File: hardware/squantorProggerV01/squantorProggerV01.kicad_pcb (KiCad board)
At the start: 2 copper layers, 29 x 29 mm, 4 parts

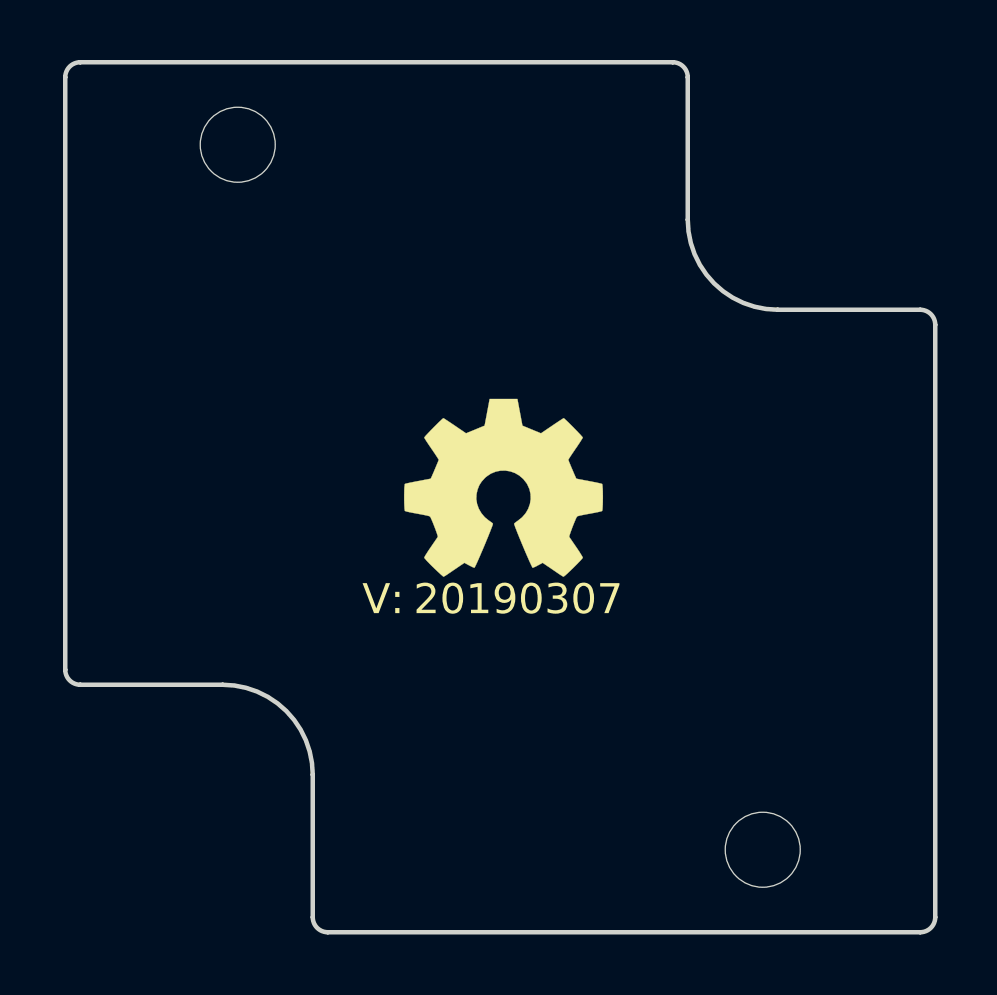
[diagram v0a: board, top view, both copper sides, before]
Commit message: placed connectors
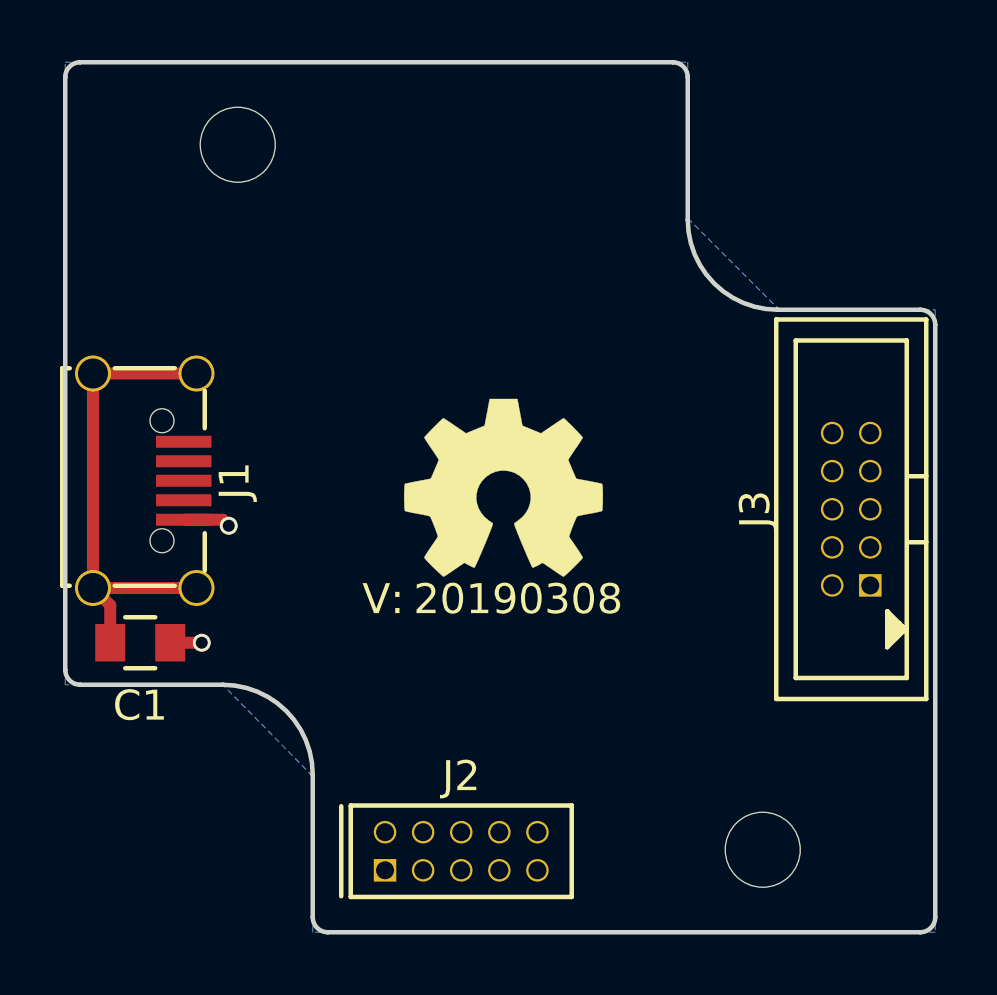
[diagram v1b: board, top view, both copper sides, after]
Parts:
- added C1: 100n, SquantorRcl:C_0805, F.Cu at (135.9, 106.2)
- added J1: USB-ID, SquantorUsb:USB-muB-SMD_TH, F.Cu at (136.1, 100.8)
- added J2: JTAG_2X05_IN, SquantorConnectors:Header-0127-2X05-H006, F.Cu at (146.6, 113.1)
- added J3: JTAG_2X05_OUT, SquantorConnectors:Header-Shr-0127-2X05-H006, F.Cu at (159.6, 101.7)
- N2: value 20190307 -> 20190308
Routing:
- net Net-(C1-Pad2): track 0.00 -> 16.1 mm
- net VSS: track 0.00 -> 2.63 mm, vias 0 -> 2
- added copper zone on B.Cu, net VSS
